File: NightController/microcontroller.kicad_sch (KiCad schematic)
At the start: 0 parts

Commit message: Add parts
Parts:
- added J203: Conn_ST_STDC14, symbol Connector:Conn_ST_STDC14
- added U201: STM32U585CIUx, Package_DFN_QFN:QFN-48-1EP_7x7mm_P0.5mm_EP5.6x5.6mm, symbol MCU_ST_STM32U5:STM32U585CIUx
- added U202: AT25SF081-SSHD-X, Package_SO:SOIC-8_3.9x4.9mm_P1.27mm, symbol Memory_Flash:AT25SF081-SSHD-X
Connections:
- new net: J203.5 (GND), J203.7 (GND)
- new net: U201.23 (VSS), U201.35 (VSS), U201.47 (VSS), U201.49 (VSS)

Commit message: Add new symbol
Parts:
- added C1, C8: 4.7uF 25V, symbol Device:C
- added C2, C3, C4, C5, C6, C9: 100nF 25V, symbol Device:C
- added C7: 10uF 25V, symbol Device:C
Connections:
- net ~{FLASH_CS}: now reaches U202.1 (~{CS})
- net ~{FLASH_CS}: now also U201.12 (PA2)
- net FLASH_IO1: now reaches U202.2 (SO/IO1)
- net FLASH_IO1: now also U201.18 (PB0)
- net FLASH_IO2: now reaches U202.3 (~{WP}/IO2)
- net FLASH_IO2: now also U201.17 (PA7)
- net GND: now reaches U202.4 (GND)
- net GND: now also J203.11 (GNDDetect), J203.5 (GND), J203.7 (GND), U201.23 (VSS), U201.35 (VSS), U201.47 (VSS), U201.49 (VSS), U201.8 (VSSA), C1.2, C2.2, C3.2, C4.2, C5.2, C6.2, C7.2, C8.2, C9.2
- net FLASH_IO0: now reaches U202.5 (SI/IO0)
- net FLASH_IO0: now also U201.19 (PB1)
- net FLASH_SCK: now reaches U202.6 (SCK)
- net FLASH_SCK: now also U201.13 (PA3)
- net FLASH_IO3: now reaches U202.7 (~{HOLD}/IO3)
- net FLASH_IO3: now also U201.16 (PA6)
- net +3.3V: now reaches U202.8 (VCC)
- net +3.3V: now also J203.3 (VCC), U201.1 (VBAT), U201.24 (VDD), U201.36 (VDD), U201.48 (VDD), U201.9 (VDDA), C1.1, C2.1, C3.1, C4.1, C5.1, C6.1, C8.1, C9.1
- net ~{NRST}: now reaches J203.12 (~{RST})
- net ~{NRST}: now also U201.7 (NRST)
- net USART1_RX: now reaches J203.13 (VCP_RX)
- net USART1_RX: now also U201.31 (PA10)
- net USART1_TX: now reaches J203.14 (VCP_TX)
- net USART1_TX: now also U201.30 (PA9)
- net SWDIO: now reaches J203.4 (JTMS/SWDIO)
- net SWDIO: now also U201.34 (PA13)
- net SWCLK: now reaches J203.6 (JCLK/SWCLK)
- net SWCLK: now also U201.37 (PA14)
- net SWO: now reaches J203.8 (JTDO/SWO)
- net SWO: now also U201.39 (PB3)
- net at U201.22 (VCAP): now also C7.1
- net USB_D_N: now reaches U201.32 (PA11)
- net USB_D_P: now reaches U201.33 (PA12)
- net DOUT: now reaches U201.40 (PB4)
- net DIN: now reaches U201.41 (PB5)
- no-connect marks 0 -> 2
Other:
- moved on the sheet: J203, U202

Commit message: Working on schematic
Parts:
- added D201: LED_ABGR, symbol Device:LED_ABGR
- added R201, R202, R203: R, symbol Device:R
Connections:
- net +3.3V: now also D201.1 (A)
- net LED_R: now reaches U201.2 (PC13)
- net LED_R: now also R201.2
- net LED_G: now reaches U201.3 (PC14)
- net LED_G: now also R202.2
- net LED_B: now reaches U201.4 (PC15)
- net LED_B: now also R203.2
- new net: D201.4 (RK), R201.1
- new net: D201.2 (BK), R203.1
- new net: D201.3 (GK), R202.1
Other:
- note added: "Status LED"

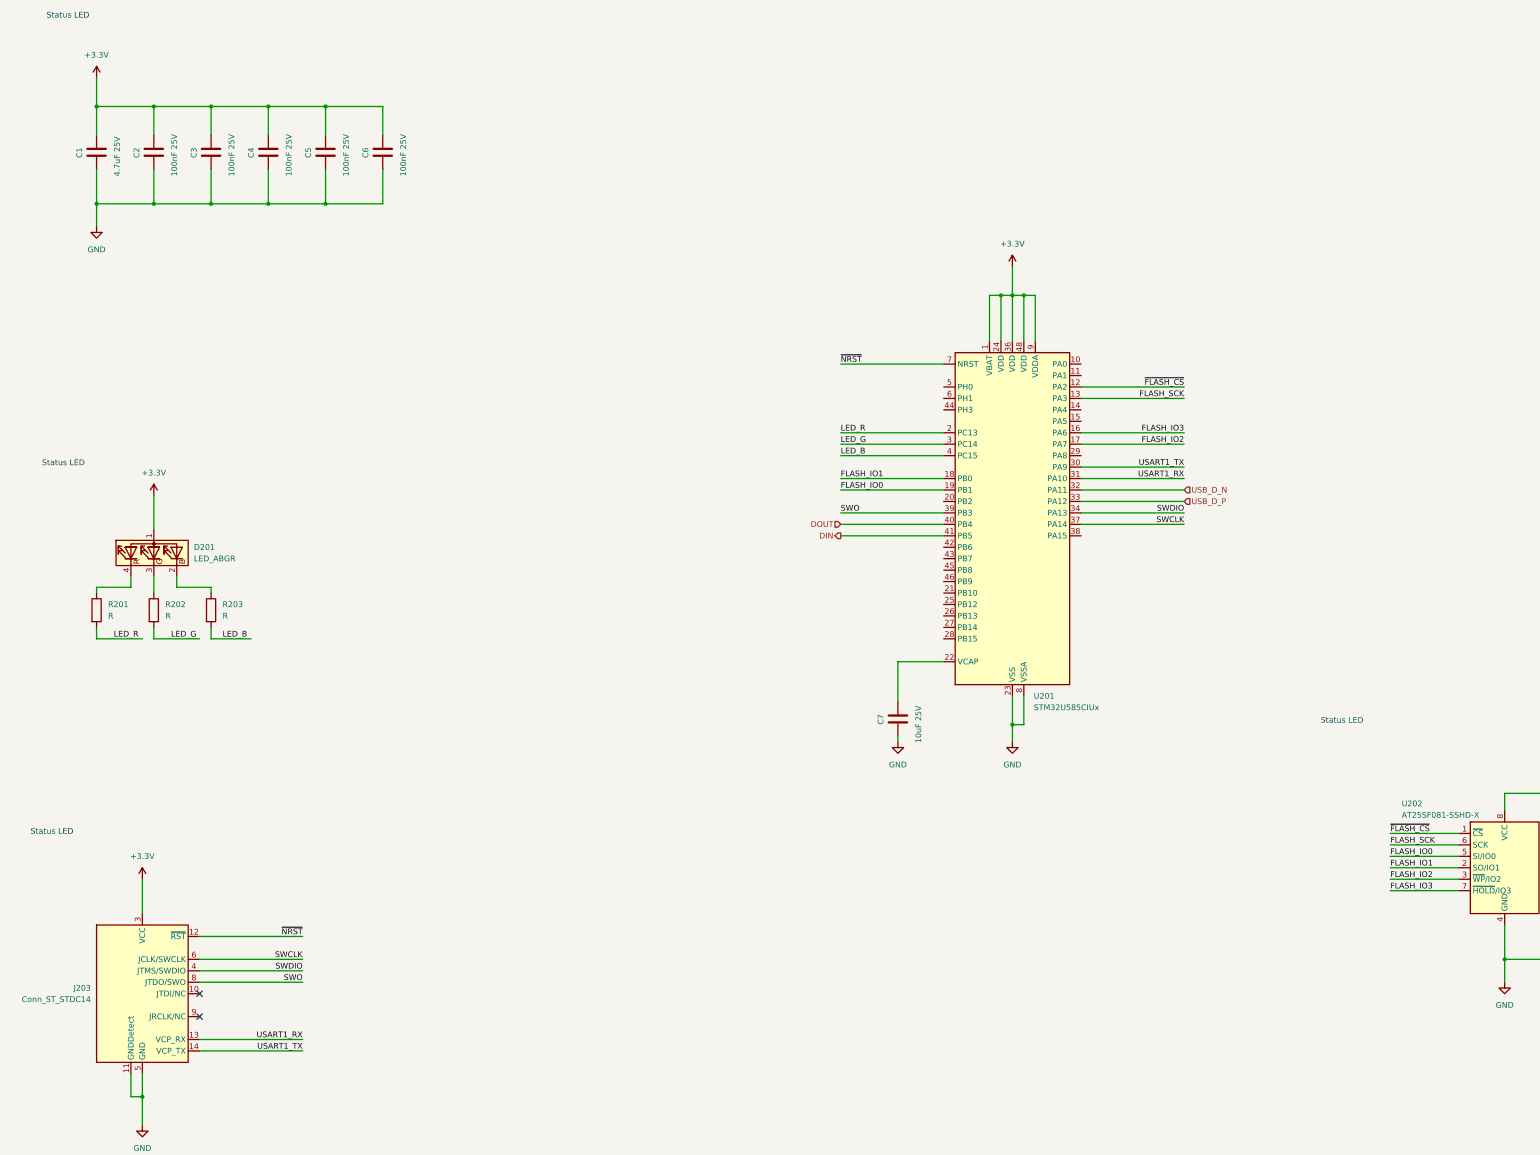
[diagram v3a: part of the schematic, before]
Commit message: update schematic
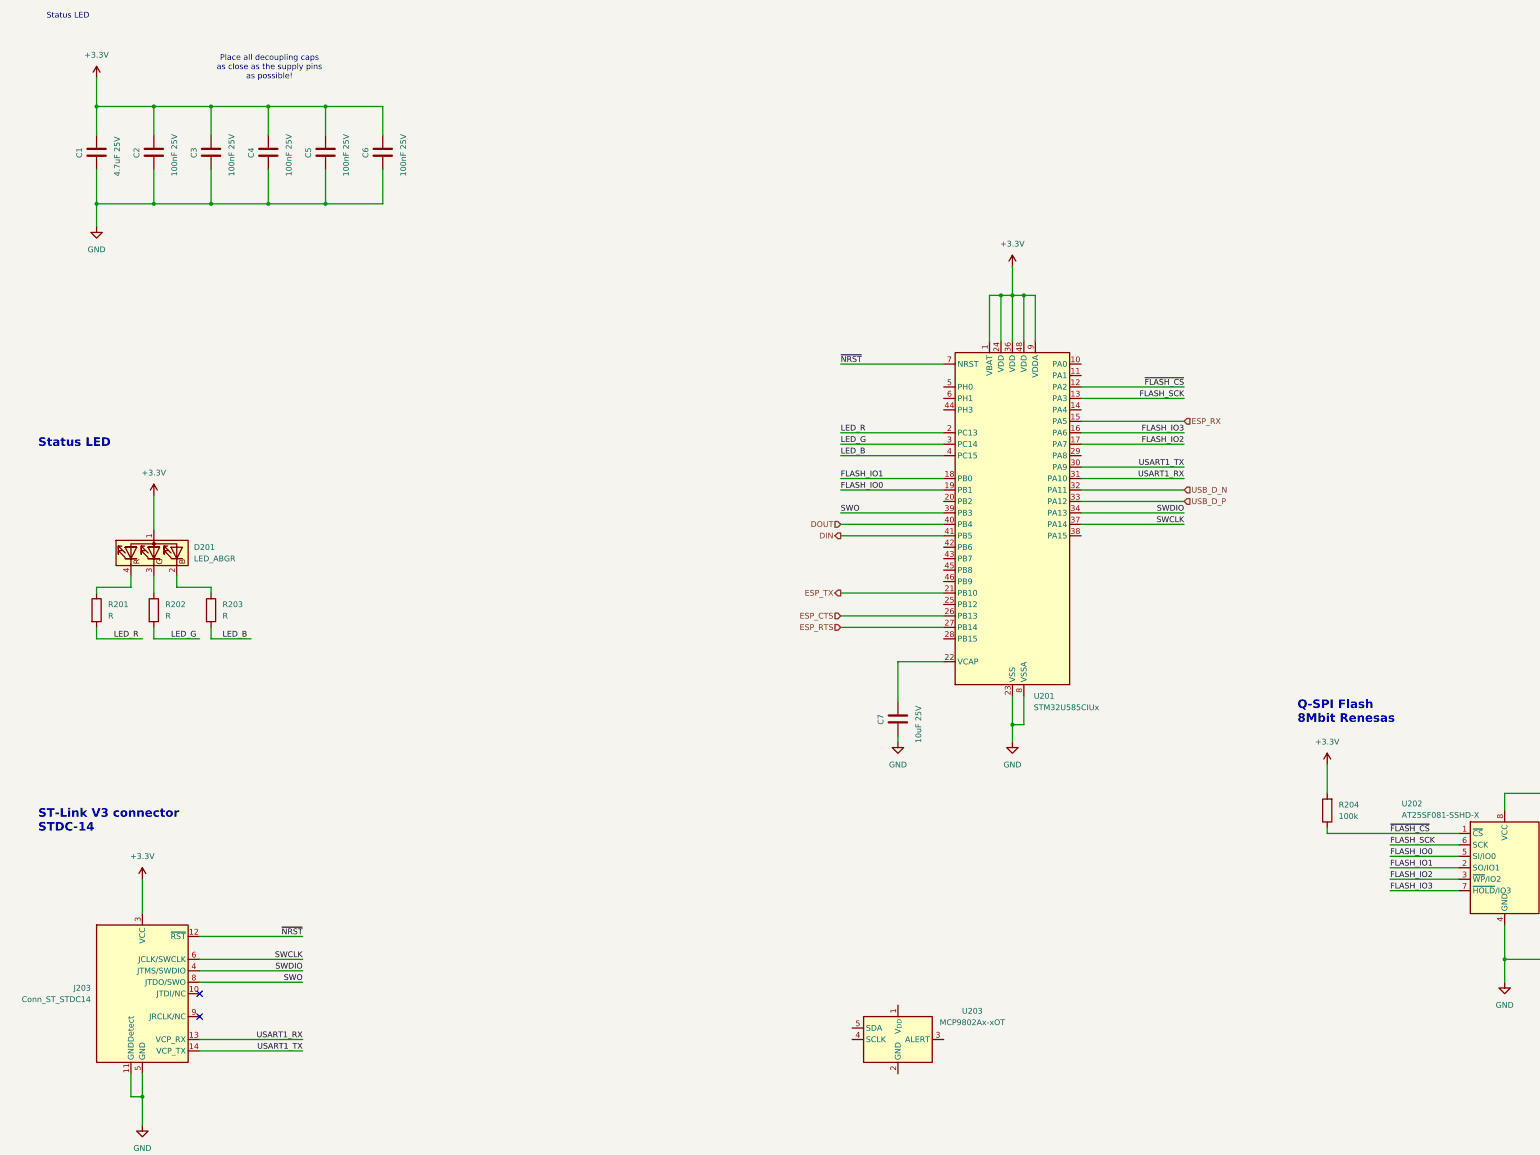
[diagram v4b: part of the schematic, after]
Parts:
- added R204: 100k, Resistor_SMD:R_0402_1005Metric_Pad0.72x0.64mm_HandSolder, symbol Device:R
- added U203: MCP9802Ax-xOT, Package_TO_SOT_SMD:SOT-23-5, symbol Sensor_Temperature:MCP9802Ax-xOT
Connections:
- net +3.3V: now also R204.2
- net ~{FLASH_CS}: now also R204.1
- net ESP_RX: now reaches U201.15 (PA5)
- net ESP_TX: now reaches U201.21 (PB10)
- net ESP_CTS: now reaches U201.26 (PB13)
- net ESP_RTS: now reaches U201.27 (PB14)
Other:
- note added: "Place all decoupling caps as close as the supply pins as possible!"
- note added: "Q-SPI Flash 8Mbit Renesas"
- note added: "ST-Link V3 connector STDC-14"

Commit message: Update microcontroller.kicad_sch
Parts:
- added C201: 10uF 25V, symbol Device:C
- added R205, R206: 4.7k 5%, symbol Device:R
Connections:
- net +3.3V: now also U203.1 (V_{DD}), C201.1, R205.1, R206.1
- net GND: now also U203.2 (GND), C201.2
- net ~{TEMP_ALT}: now reaches U203.3 (ALERT)
- net ~{TEMP_ALT}: now also U201.43 (PB7)
- net TEMP_SCL: now reaches U203.4 (SCLK)
- net TEMP_SCL: now also U201.45 (PB8), R206.2
- net TEMP_SDA: now reaches U203.5 (SDA)
- net TEMP_SDA: now also U201.46 (PB9), R205.2

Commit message: Finished mcu
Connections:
- net DIN: now also U201.10 (PA0); no longer U201.41 (PB5)
- net DOUT: now also U201.11 (PA1); no longer U201.40 (PB4)
- net ESP_CTS: now also U201.40 (PB4); no longer U201.26 (PB13)
- net ESP_RTS: now also U201.39 (PB3); no longer U201.27 (PB14)
- net ESP_RX: now also U201.43 (PB7); no longer U201.15 (PA5)
- net ESP_TX: now also U201.42 (PB6); no longer U201.21 (PB10)
- net SWO: no longer U201.39 (PB3)
- net USART1_RX: no longer U201.31 (PA10)
- net USART1_TX: no longer U201.30 (PA9)
- net ~{FLASH_CS}: now also U201.14 (PA4); no longer U201.12 (PA2)
- net ~{TEMP_ALT}: now also U201.41 (PB5); no longer U201.43 (PB7)
- new net USART3_RX: U201.15 (PA5)
- new net USART3_TX: U201.21 (PB10)
- new net USB_VBUS_SENS: U201.30 (PA9)
- no-connect marks 2 -> 10
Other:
- note added: "Temperature Sensor"
